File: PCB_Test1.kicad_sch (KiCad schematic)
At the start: 3 parts

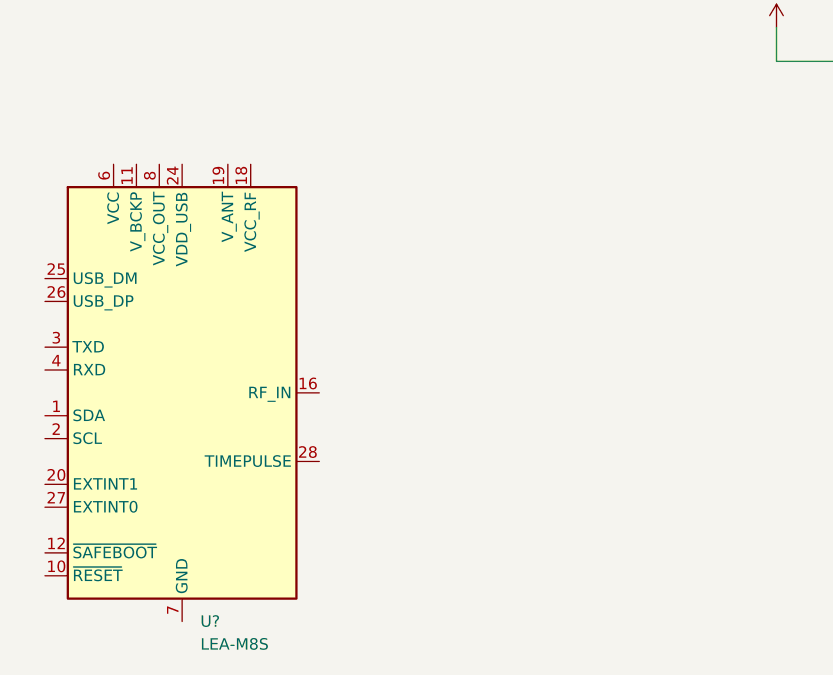
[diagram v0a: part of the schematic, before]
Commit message: Add L70-R GPS module to schematic
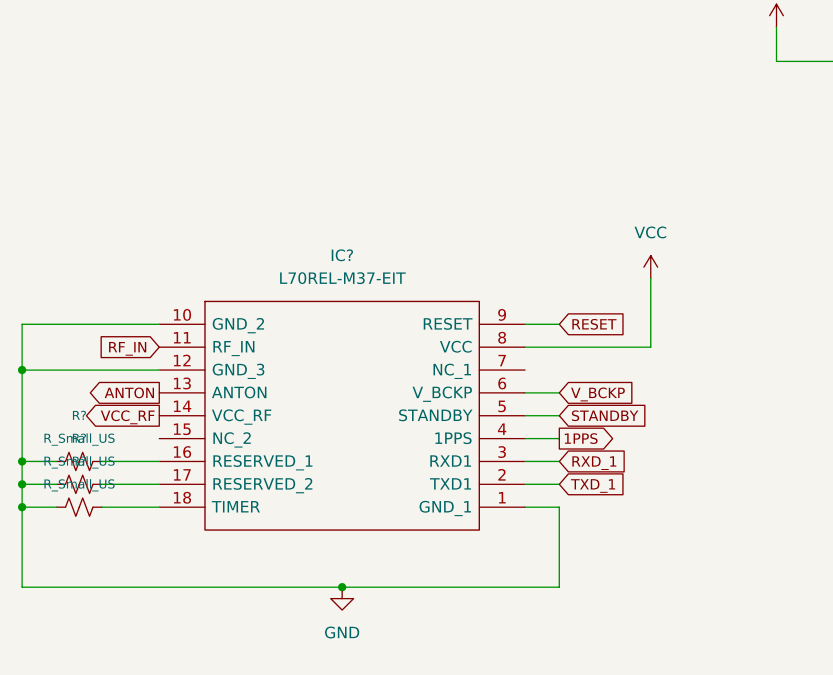
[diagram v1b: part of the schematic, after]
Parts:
- removed U?: LEA-M8S, RF_GPS:ublox_LEA, symbol RF_GPS:LEA-M8S
- added IC?: L70REL-M37-EIT, L70RELM37EIT, symbol GPS Module:L70REL-M37-EIT
- added R? (x3): R_Small_US, symbol Device:R_Small_US
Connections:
- net GND: now also IC?.1 (GND_1), IC?.10 (GND_2), IC?.12 (GND_3), R?.1, R?.1, R?.1
- new net: IC?.16 (RESERVED_1), R?.2
- new net: IC?.18 (TIMER), R?.2
- new net: IC?.17 (RESERVED_2), R?.2
- new net 1PPS: IC?.4 (1PPS)
- new net ANTON: IC?.13 (ANTON)
- new net RESET: IC?.9 (RESET)
- new net RF_IN: IC?.11 (RF_IN)
- new net RXD_1: IC?.3 (RXD1)
- new net STANDBY: IC?.5 (STANDBY)
- new net TXD_1: IC?.2 (TXD1)
- new net VCC: IC?.8 (VCC)
- new net VCC_RF: IC?.14 (VCC_RF)
- new net V_BCKP: IC?.6 (V_BCKP)

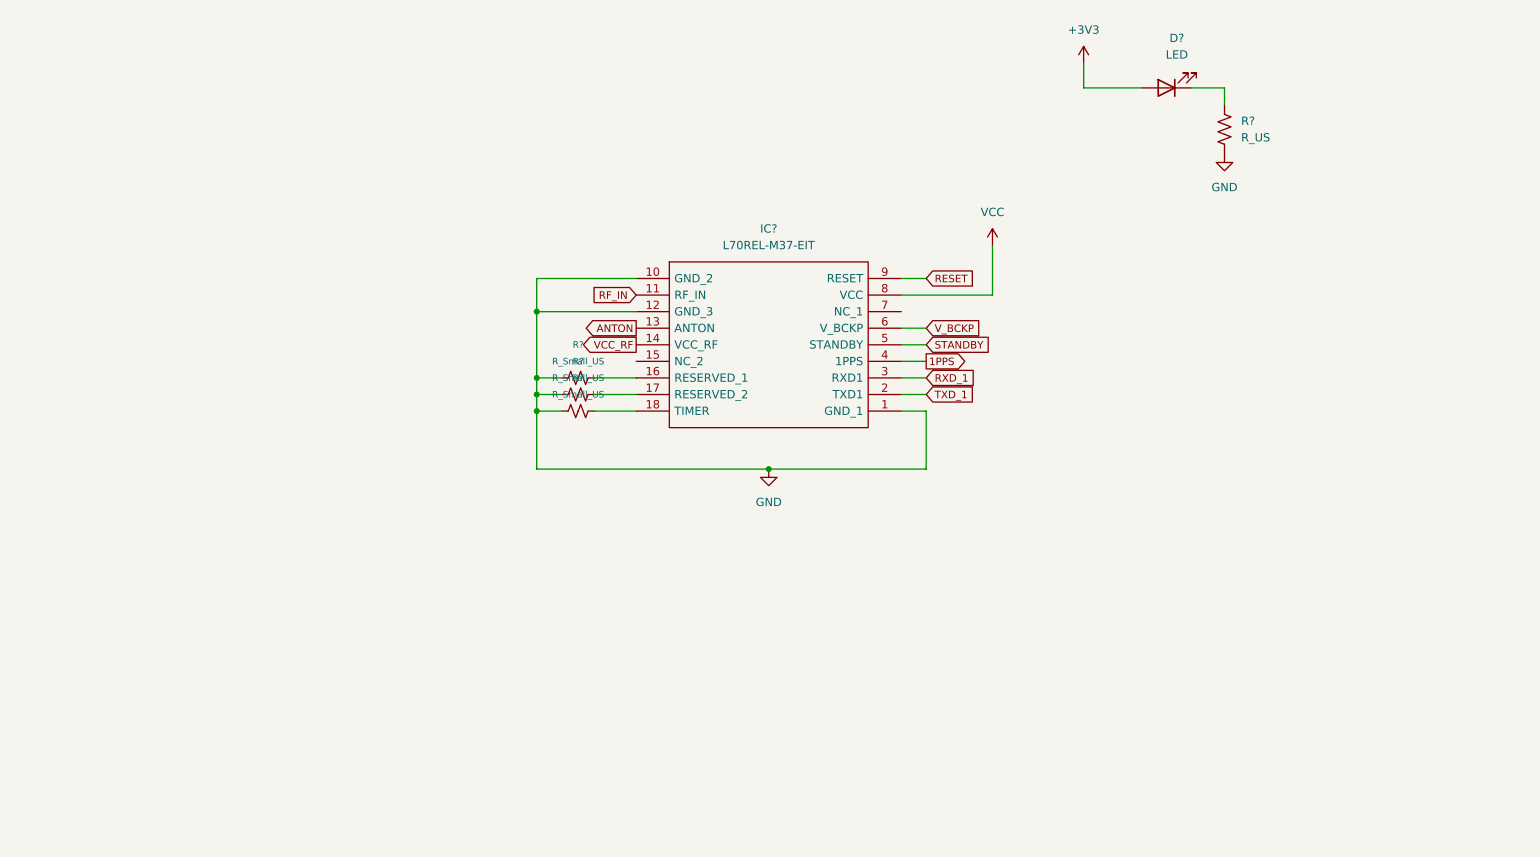
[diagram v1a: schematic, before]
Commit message: Add Arduino to schematic
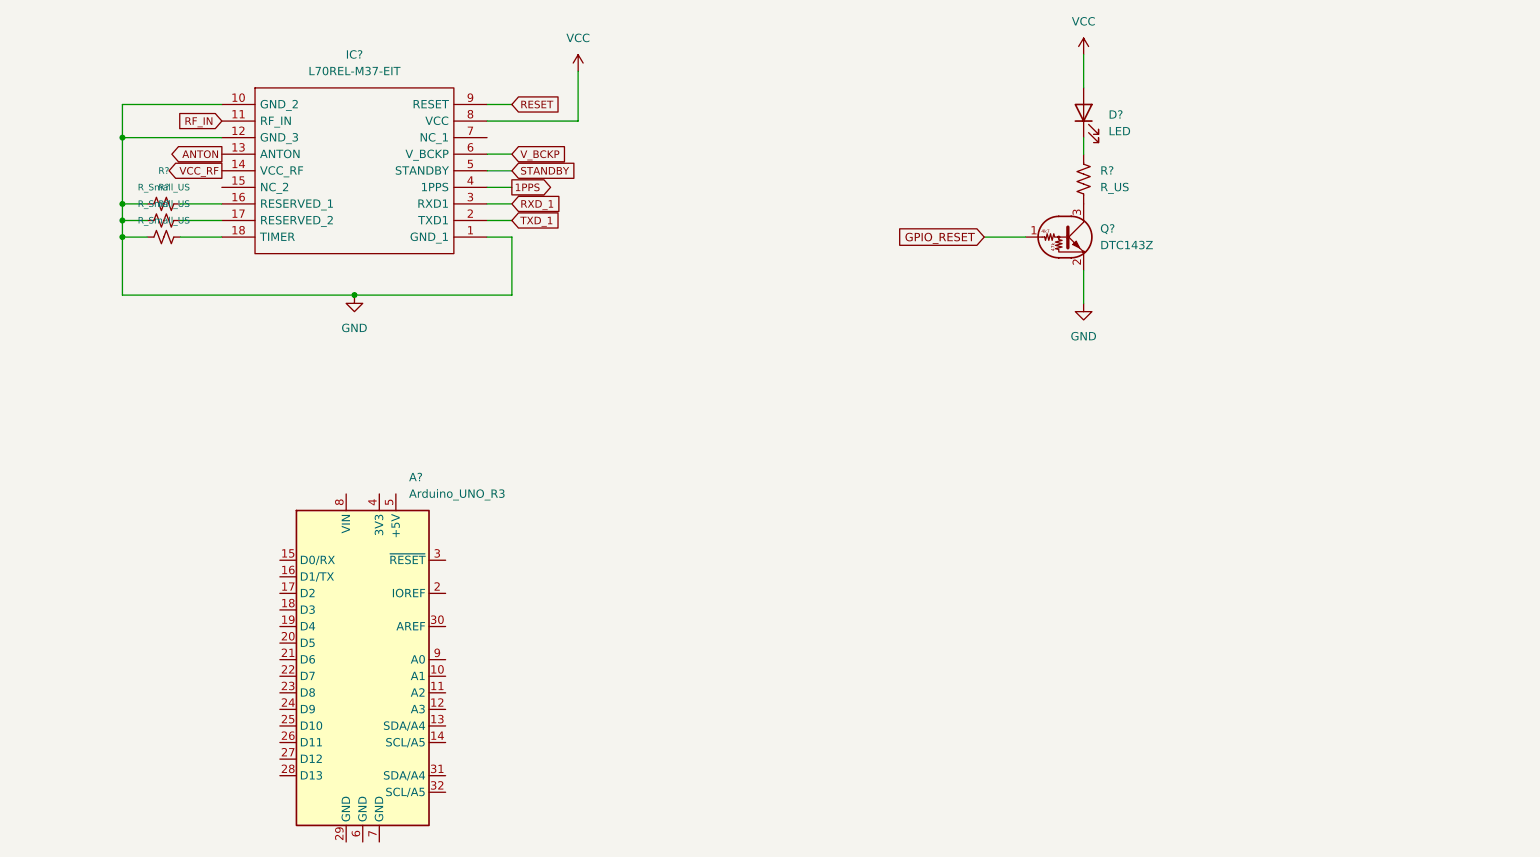
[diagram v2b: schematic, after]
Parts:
- added A?: Arduino_UNO_R3, Module:Arduino_UNO_R3, symbol MCU_Module:Arduino_UNO_R3
- added Q?: DTC143Z, symbol Transistor_BJT:DTC143Z
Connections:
- net +3V3 is gone; now on net VCC: D?.2 (A)
- net GND: now also Q?.2 (E); no longer R?.2
- new net: Q?.3 (C), R?.2
- new net GPIO_RESET: Q?.1 (B)
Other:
- moved on the sheet: D?, IC?, R?

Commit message: Assign footprints
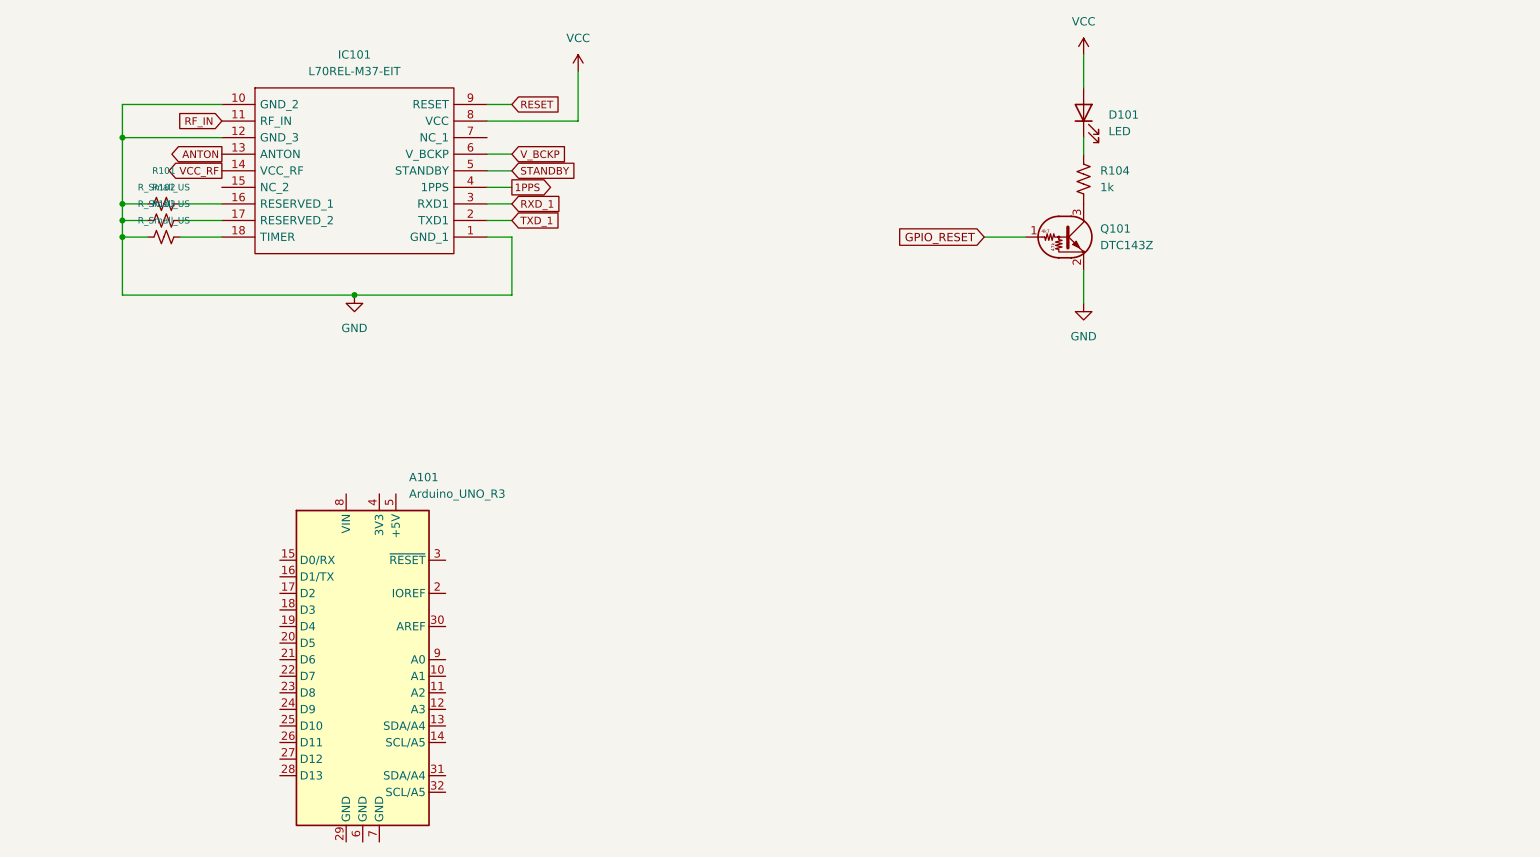
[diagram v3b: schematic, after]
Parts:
- D101: renamed from D?; footprint (none) -> LED_SMD:LED_1210_3225Metric
- IC101: renamed from IC?; footprint L70RELM37EIT -> L70REL-M37-EIT:L70RELM37EIT
- Q101: renamed from Q?; footprint (none) -> Package_TO_SOT_SMD:SOT-416
- R101, R102, R103: renamed from R?; footprint (none) -> Resistor_SMD:R_1206_3216Metric
- R104: renamed from R?; value R_US -> 1k; footprint (none) -> Resistor_SMD:R_1206_3216Metric
- gave numbers to parts that had none: 1
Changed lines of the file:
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@@
   (symbol (lib_id "power:GND") (at 71.12 76.2 0) (unit 1)
     (in_bom yes) (on_board yes) (fields_autoplaced)
-    (property "Reference" "#PWR?" (id 0) (at 71.12 82.55 0)
+    (property "Reference" "#PWR0102" (id 0) (at 71.12 82.55 0)
       (effects (font (size 1.27 1.27)) hide)
     )
@@
   (symbol (lib_id "Device:LED") (at 182.88 48.26 90) (unit 1)
     (in_bom yes) (on_board yes)
-    (property "Reference" "D?" (id 0) (at 186.69 48.5774 90)
+    (property "Reference" "D101" (id 0) (at 186.69 48.5774 90)
       (effects (font (size 1.27 1.27)) (justify right))
     )
@@
       (effects (font (size 1.27 1.27)) (justify right))
     )
-    (property "Footprint" "" (id 2) (at 182.88 48.26 0)
+    (property "Footprint" "LED_SMD:LED_1210_3225Metric" (id 2) (at 182.88 48.26 0)
       (effects (font (size 1.27 1.27)) hide)
     )
@@
   (symbol (lib_id "Device:R_Small_US") (at 41.91 62.23 90) (unit 1)
     (in_bom yes) (on_board yes) (fields_autoplaced)
-    (property "Reference" "R?" (id 0) (at 41.91 57.15 90)
+    (property "Reference" "R101" (id 0) (at 41.91 57.15 90)
       (effects (font (size 1 1)))
     )
@@
       (effects (font (size 1 1)))
     )
-    (property "Footprint" "" (id 2) (at 41.91 62.23 0)
+    (property "Footprint" "Resistor_SMD:R_1206_3216Metric" (id 2) (at 41.91 62.23 0)
       (effects (font (size 1.27 1.27)) hide)
     )
@@
   (symbol (lib_id "MCU_Module:Arduino_UNO_R3") (at 72.39 132.08 0) (unit 1)
     (in_bom yes) (on_board yes) (fields_autoplaced)
-    (property "Reference" "A?" (id 0) (at 79.4894 104.14 0)
+    (property "Reference" "A101" (id 0) (at 79.4894 104.14 0)
       (effects (font (size 1.27 1.27)) (justify left))
     )
@@
   (symbol (lib_id "Device:R_Small_US") (at 41.91 67.31 90) (unit 1)
     (in_bom yes) (on_board yes)
-    (property "Reference" "R?" (id 0) (at 41.91 62.23 90)
+    (property "Reference" "R103" (id 0) (at 41.91 62.23 90)
       (effects (font (size 1 1)))
     )
@@
       (effects (font (size 1 1)))
     )
-    (property "Footprint" "" (id 2) (at 41.91 67.31 0)
+    (property "Footprint" "Resistor_SMD:R_1206_3216Metric" (id 2) (at 41.91 67.31 0)
       (effects (font (size 1.27 1.27)) hide)
     )
@@
   (symbol (lib_id "power:VCC") (at 182.88 39.37 0) (unit 1)
     (in_bom yes) (on_board yes) (fields_autoplaced)
-    (property "Reference" "#PWR?" (id 0) (at 182.88 43.18 0)
+    (property "Reference" "#PWR0104" (id 0) (at 182.88 43.18 0)
       (effects (font (size 1.27 1.27)) hide)
     )
@@
   (symbol (lib_id "Transistor_BJT:DTC143Z") (at 180.34 67.31 0) (unit 1)
     (in_bom yes) (on_board yes) (fields_autoplaced)
-    (property "Reference" "Q?" (id 0) (at 185.42 66.0399 0)
+    (property "Reference" "Q101" (id 0) (at 185.42 66.0399 0)
       (effects (font (size 1.27 1.27)) (justify left))
     )
@@
       (effects (font (size 1.27 1.27)) (justify left))
     )
-    (property "Footprint" "" (id 2) (at 180.34 67.31 0)
+    (property "Footprint" "Package_TO_SOT_SMD:SOT-416" (id 2) (at 180.34 67.31 0)
       (effects (font (size 1.27 1.27)) (justify left) hide)
     )
@@
   (symbol (lib_id "GPS Module:L70REL-M37-EIT") (at 50.8 46.99 0) (unit 1)
     (in_bom yes) (on_board yes) (fields_autoplaced)
-    (property "Reference" "IC?" (id 0) (at 71.12 39.37 0))
+    (property "Reference" "IC101" (id 0) (at 71.12 39.37 0))
     (property "Value" "L70REL-M37-EIT" (id 1) (at 71.12 41.91 0))
-    (property "Footprint" "L70RELM37EIT" (id 2) (at 87.63 44.45 0)
+    (property "Footprint" "L70REL-M37-EIT:L70RELM37EIT" (id 2) (at 87.63 44.45 0)
       (effects (font (size 1.27 1.27)) (justify left) hide)
     )
@@
   (symbol (lib_id "power:VCC") (at 105.41 41.91 0) (unit 1)
     (in_bom yes) (on_board yes) (fields_autoplaced)
-    (property "Reference" "#PWR?" (id 0) (at 105.41 45.72 0)
+    (property "Reference" "#PWR0103" (id 0) (at 105.41 45.72 0)
       (effects (font (size 1.27 1.27)) hide)
     )
@@
   (symbol (lib_id "Device:R_US") (at 182.88 58.42 0) (unit 1)
     (in_bom yes) (on_board yes)
-    (property "Reference" "R?" (id 0) (at 185.42 57.1499 0)
-      (effects (font (size 1.27 1.27)) (justify left))
-    )
-    (property "Value" "R_US" (id 1) (at 185.42 59.6899 0)
-      (effects (font (size 1.27 1.27)) (justify left))
-    )
-    (property "Footprint" "" (id 2) (at 183.896 58.674 90)
+    (property "Reference" "R104" (id 0) (at 185.42 57.1499 0)
+      (effects (font (size 1.27 1.27)) (justify left))
+    )
+    (property "Value" "1k" (id 1) (at 185.42 59.6899 0)
+      (effects (font (size 1.27 1.27)) (justify left))
+    )
+    (property "Footprint" "Resistor_SMD:R_1206_3216Metric" (id 2) (at 183.896 58.674 90)
       (effects (font (size 1.27 1.27)) hide)
     )
@@
   (symbol (lib_id "Device:R_Small_US") (at 41.91 64.77 90) (unit 1)
     (in_bom yes) (on_board yes) (fields_autoplaced)
-    (property "Reference" "R?" (id 0) (at 41.91 59.69 90)
+    (property "Reference" "R102" (id 0) (at 41.91 59.69 90)
       (effects (font (size 1 1)))
     )
@@
       (effects (font (size 1 1)))
     )
-    (property "Footprint" "" (id 2) (at 41.91 64.77 0)
+    (property "Footprint" "Resistor_SMD:R_1206_3216Metric" (id 2) (at 41.91 64.77 0)
       (effects (font (size 1.27 1.27)) hide)
     )
@@
     )
     (path "/065211f6-6826-4b56-97d7-571e8e253797"
-      (reference "#PWR?") (unit 1) (value "GND") (footprint "")
+      (reference "#PWR0102") (unit 1) (value "GND") (footprint "")
+    )
+    (path "/d7f3eb6a-aef9-4b1f-b472-f34135c0d830"
+      (reference "#PWR0103") (unit 1) (value "VCC") (footprint "")
     )
     (path "/a3a21585-fd73-4e55-b17d-ca320a4df49d"
-      (reference "#PWR?") (unit 1) (value "VCC") (footprint "")
-    )
-    (path "/d7f3eb6a-aef9-4b1f-b472-f34135c0d830"
-      (reference "#PWR?") (unit 1) (value "VCC") (footprint "")
+      (reference "#PWR0104") (unit 1) (value "VCC") (footprint "")
     )
     (path "/577d95df-df73-428a-8f02-e461f346fc7b"
-      (reference "A?") (unit 1) (value "Arduino_UNO_R3") (footprint "Module:Arduino_UNO_R3")
+      (reference "A101") (unit 1) (value "Arduino_UNO_R3") (footprint "Module:Arduino_UNO_R3")
     )
     (path "/43cc368e-4915-491d-a959-587ee1a58f20"
-      (reference "D?") (unit 1) (value "LED") (footprint "")
+      (reference "D101") (unit 1) (value "LED") (footprint "LED_SMD:LED_1210_3225Metric")
     )
     (path "/cf0bbd0d-22ee-4ea7-9877-80945221f044"
-      (reference "IC?") (unit 1) (value "L70REL-M37-EIT") (footprint "L70RELM37EIT")
+      (reference "IC101") (unit 1) (value "L70REL-M37-EIT") (footprint "L70REL-M37-EIT:L70RELM37EIT")
     )
     (path "/bed616db-93c6-4861-83b1-5be85445fb75"
-      (reference "Q?") (unit 1) (value "DTC143Z") (footprint "")
+      (reference "Q101") (unit 1) (value "DTC143Z") (footprint "Package_TO_SOT_SMD:SOT-416")
     )
     (path "/4dc54989-4adb-4c88-ac5e-0741877f7a3c"
-      (reference "R?") (unit 1) (value "R_Small_US") (footprint "")
+      (reference "R101") (unit 1) (value "R_Small_US") (footprint "Resistor_SMD:R_1206_3216Metric")
+    )
+    (path "/eed8d599-3c89-4ec9-9236-2bd0f5fd6e8a"
+      (reference "R102") (unit 1) (value "R_Small_US") (footprint "Resistor_SMD:R_1206_3216Metric")
     )
     (path "/9669849d-9831-472c-bdba-8c077c81c6ad"
-      (reference "R?") (unit 1) (value "R_Small_US") (footprint "")
+      (reference "R103") (unit 1) (value "R_Small_US") (footprint "Resistor_SMD:R_1206_3216Metric")
     )
     (path "/dccaa679-56a5-4109-b744-515d53cc66b4"
-      (reference "R?") (unit 1) (value "R_US") (footprint "")
-    )
-    (path "/eed8d599-3c89-4ec9-9236-2bd0f5fd6e8a"
-      (reference "R?") (unit 1) (value "R_Small_US") (footprint "")
-    )
-  )
+      (reference "R104") (unit 1) (value "1k") (footprint "Resistor_SMD:R_1206_3216Metric")
+    )
+  )
